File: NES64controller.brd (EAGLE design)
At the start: 113 x 45.7 mm, 10 parts, among them CN1 NES64_CONNECTOR

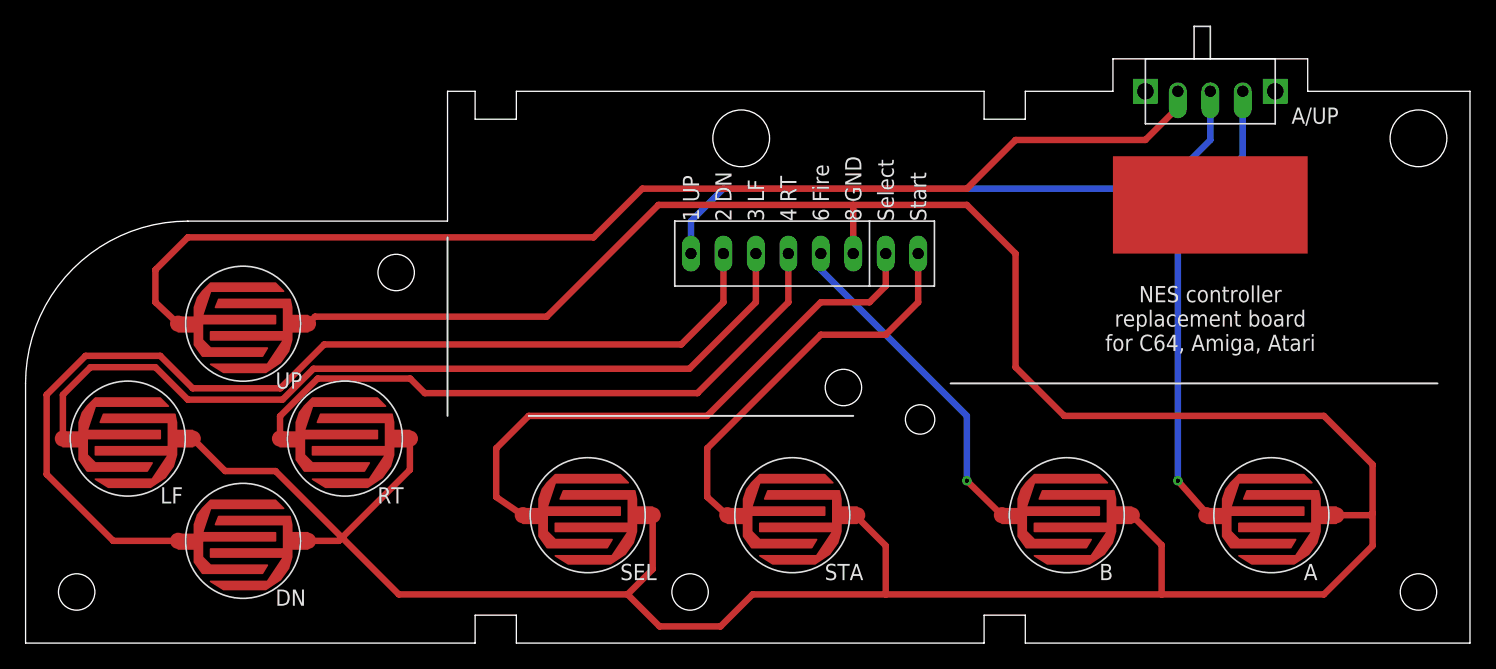
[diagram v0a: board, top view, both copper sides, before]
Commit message: Adjustment of hole size in lower right corner and edge notches to fit USB controller case; slight correcting translation of top holes and middle small hole downwards; removing small area of solder mask from middle of button contact areas; adjusting distance between switch pads
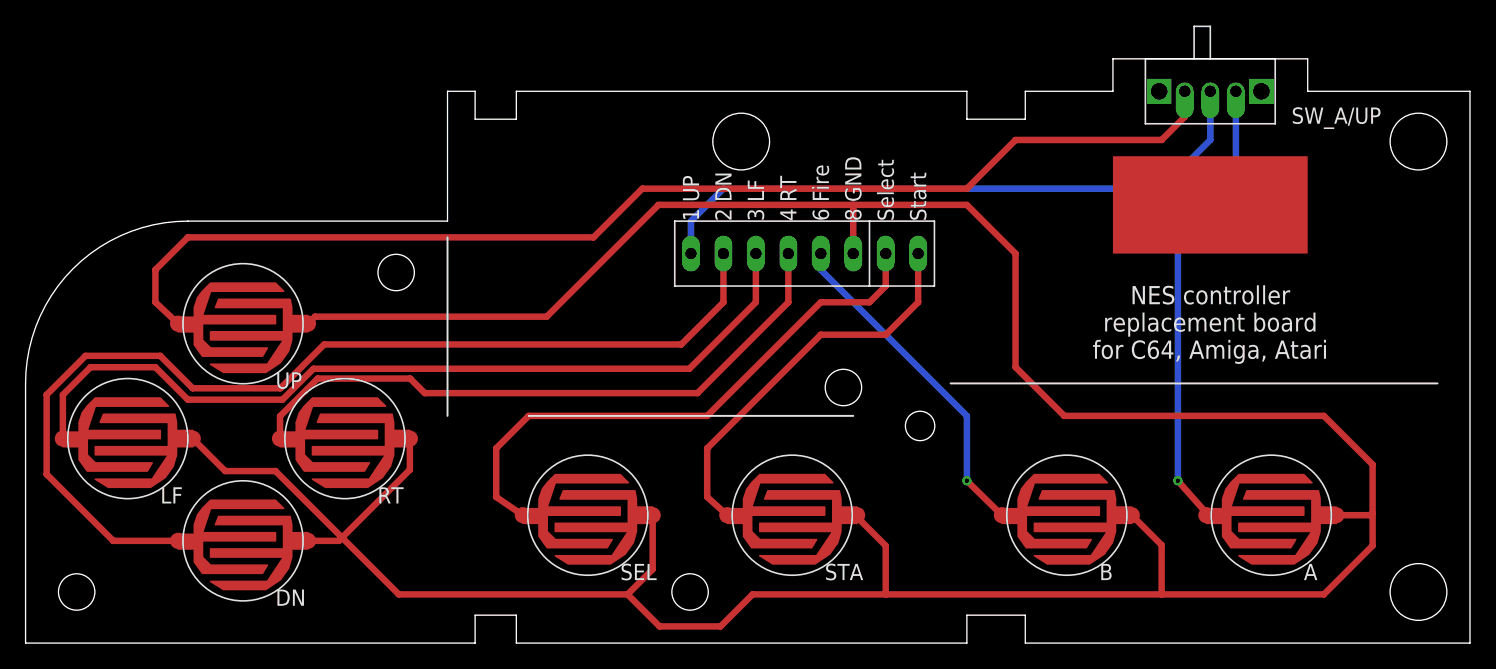
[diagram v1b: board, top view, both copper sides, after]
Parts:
- renumbered A/UP to SW_A/UP
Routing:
- net N$9: track 91.5 -> 92.5 mm
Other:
- outline, holes or cut-outs redrawn
- board text added: "version 0.2"
- board text removed: "version 0.1"
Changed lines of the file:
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@@
 <layers>
 <layer number="1" name="Top" color="4" fill="1" visible="yes" active="yes"/>
-<layer number="16" name="Bottom" color="1" fill="1" visible="no" active="yes"/>
+<layer number="16" name="Bottom" color="1" fill="1" visible="yes" active="yes"/>
 <layer number="17" name="Pads" color="2" fill="1" visible="yes" active="yes"/>
 <layer number="18" name="Vias" color="2" fill="1" visible="yes" active="yes"/>
@@
 <layer number="20" name="Dimension" color="24" fill="1" visible="yes" active="yes"/>
 <layer number="21" name="tPlace" color="7" fill="1" visible="yes" active="yes"/>
-<layer number="22" name="bPlace" color="7" fill="1" visible="no" active="yes"/>
+<layer number="22" name="bPlace" color="7" fill="1" visible="yes" active="yes"/>
 <layer number="23" name="tOrigins" color="15" fill="1" visible="yes" active="yes"/>
-<layer number="24" name="bOrigins" color="15" fill="1" visible="no" active="yes"/>
+<layer number="24" name="bOrigins" color="15" fill="1" visible="yes" active="yes"/>
 <layer number="25" name="tNames" color="7" fill="1" visible="yes" active="yes"/>
-<layer number="26" name="bNames" color="7" fill="1" visible="no" active="yes"/>
+<layer number="26" name="bNames" color="7" fill="1" visible="yes" active="yes"/>
 <layer number="27" name="tValues" color="7" fill="1" visible="yes" active="yes"/>
-<layer number="28" name="bValues" color="7" fill="1" visible="no" active="yes"/>
+<layer number="28" name="bValues" color="7" fill="1" visible="yes" active="yes"/>
 <layer number="29" name="tStop" color="7" fill="3" visible="yes" active="yes"/>
 <layer number="30" name="bStop" color="7" fill="6" visible="no" active="yes"/>
@@
 <wire x1="35.179" y1="2.1844" x2="38.4048" y2="2.1844" width="0" layer="20"/>
 <wire x1="38.4048" y1="2.1844" x2="38.4048" y2="0" width="0" layer="20"/>
-<wire x1="38.4048" y1="0" x2="75.0062" y2="0" width="0" layer="20"/>
-<wire x1="75.0062" y1="0" x2="75.0062" y2="2.1844" width="0" layer="20"/>
-<wire x1="75.0062" y1="2.1844" x2="78.232" y2="2.1844" width="0" layer="20"/>
+<wire x1="38.4048" y1="0" x2="73.66" y2="0" width="0" layer="20"/>
+<wire x1="73.66" y1="0" x2="73.66" y2="2.1844" width="0" layer="20"/>
+<wire x1="73.66" y1="2.1844" x2="78.232" y2="2.1844" width="0" layer="20"/>
 <wire x1="78.232" y1="2.1844" x2="78.232" y2="0" width="0" layer="20"/>
 <wire x1="78.232" y1="0" x2="113.03" y2="0" width="0" layer="20"/>
@@
 <wire x1="85.09" y1="43.18" x2="78.232" y2="43.18" width="0" layer="20"/>
 <wire x1="78.232" y1="43.18" x2="78.232" y2="40.9956" width="0" layer="20"/>
-<wire x1="78.232" y1="40.9956" x2="75.0062" y2="40.9956" width="0" layer="20"/>
-<wire x1="75.0062" y1="40.9956" x2="75.0062" y2="43.18" width="0" layer="20"/>
-<wire x1="75.0062" y1="43.18" x2="38.4048" y2="43.18" width="0" layer="20"/>
+<wire x1="78.232" y1="40.9956" x2="73.66" y2="40.9956" width="0" layer="20"/>
+<wire x1="73.66" y1="40.9956" x2="73.66" y2="43.18" width="0" layer="20"/>
+<wire x1="73.66" y1="43.18" x2="38.4048" y2="43.18" width="0" layer="20"/>
 <wire x1="38.4048" y1="43.18" x2="38.4048" y2="40.9956" width="0" layer="20"/>
 <wire x1="38.4048" y1="40.9956" x2="35.179" y2="40.9956" width="0" layer="20"/>
@@
 <hole x="4" y="4" drill="2.85"/>
 <hole x="52" y="4" drill="2.85"/>
-<hole x="109" y="4" drill="2.85"/>
-<hole x="109" y="39.5" drill="4.44"/>
-<hole x="56" y="39.5" drill="4.44"/>
+<hole x="109" y="4" drill="4.44"/>
+<hole x="109" y="39.246" drill="4.44"/>
+<hole x="56" y="39.246" drill="4.44"/>
 <hole x="29" y="29" drill="2.85"/>
 <hole x="64" y="20" drill="2.85"/>
-<hole x="70" y="17.5" drill="2.3"/>
+<hole x="70" y="16.992" drill="2.3"/>
 <wire x1="39.37" y1="17.78" x2="64.77" y2="17.78" width="0.1524" layer="21"/>
 <wire x1="72.39" y1="20.32" x2="110.49" y2="20.32" width="0.1524" layer="21"/>
 <wire x1="33.02" y1="31.75" x2="33.02" y2="17.78" width="0.1524" layer="21"/>
-<text x="92.71" y="27.94" size="1.27" layer="21" align="top-center">NES controller
+<text x="92.71" y="27.94" size="1.4224" layer="21" align="top-center">NES controller
 replacement board
 for C64, Amiga, Atari</text>
 <rectangle x1="85.09" y1="30.48" x2="100.33" y2="38.1" layer="1"/>
 <text x="92.71" y="36.83" size="2.54" layer="29" align="top-center">NES64</text>
-<text x="92.71" y="31.75" size="1.778" layer="29" align="bottom-center">version 0.1</text>
+<text x="92.71" y="31.75" size="1.778" layer="29" align="bottom-center">version 0.2</text>
 <wire x1="22.86" y1="16.51" x2="10.16" y2="16.51" width="0.508" layer="22"/>
 <wire x1="10.16" y1="16.51" x2="11.43" y2="11.43" width="0.508" layer="22"/>
@@
 <wire x1="30.48" y1="30.48" x2="50.8" y2="30.48" width="0.1524" layer="22"/>
 <text x="1.27" y="45.72" size="1.778" layer="51" align="top-left">Board thickness: 1.6 mm</text>
-<text x="106.68" y="13.97" size="1.27" layer="22" rot="MR0">For use in NES controller to make it
+<text x="106.68" y="13.97" size="1.4224" layer="22" rot="MR0">For use in NES controller to make it
 compatible with Commodore 64,
 Amiga, and other computers using
@@
 <attribute name="NAME" x="19.558" y="21.1836" size="1.27" layer="25" align="top-left"/>
 </element>
-<element name="A/UP" library="Thomas" package="TOGGLESWITCH_SPDT_SMALL_90DEG" value="TOGGLESWITCH_SPDT_SMALL_90DEG" x="92.71" y="43.18" smashed="yes">
+<element name="SW_A/UP" library="Thomas" package="TOGGLESWITCH_SPDT_SMALL_90DEG" value="TOGGLESWITCH_SPDT_SMALL_90DEG" x="92.71" y="43.18" smashed="yes">
 <attribute name="NAME" x="99.06" y="40.64" size="1.27" layer="25"/>
 </element>
@@
 <signal name="N$9">
 <contactref element="UP" pad="A"/>
-<contactref element="A/UP" pad="A"/>
+<contactref element="SW_A/UP" pad="A"/>
 <wire x1="11.938" y1="24.9936" x2="10.16" y2="26.67" width="0.508" layer="1"/>
 <wire x1="10.16" y1="29.21" x2="10.16" y2="26.67" width="0.508" layer="1"/>
-<wire x1="77.47" y1="39.37" x2="73.66" y2="35.56" width="0.508" layer="1"/>
-<wire x1="87.63" y1="39.37" x2="77.47" y2="39.37" width="0.508" layer="1"/>
-<wire x1="90.17" y1="43.18" x2="90.17" y2="41.91" width="0.508" layer="1"/>
-<wire x1="90.17" y1="41.91" x2="87.63" y2="39.37" width="0.508" layer="1"/>
+<wire x1="73.66" y1="35.56" x2="77.47" y2="39.37" width="0.508" layer="1"/>
 <wire x1="48.26" y1="35.56" x2="44.45" y2="31.75" width="0.508" layer="1"/>
 <wire x1="73.66" y1="35.56" x2="48.26" y2="35.56" width="0.508" layer="1"/>
 <wire x1="44.45" y1="31.75" x2="12.7" y2="31.75" width="0.508" layer="1"/>
 <wire x1="12.7" y1="31.75" x2="10.16" y2="29.21" width="0.508" layer="1"/>
+<wire x1="77.47" y1="39.37" x2="88.9" y2="39.37" width="0.508" layer="1"/>
+<wire x1="88.9" y1="39.37" x2="90.71" y2="41.18" width="0.508" layer="1"/>
+<wire x1="90.71" y1="41.18" x2="90.71" y2="43.18" width="0.508" layer="1"/>
 </signal>
 <signal name="N$4">
@@
 <signal name="N$10">
 <contactref element="A" pad="A"/>
-<contactref element="A/UP" pad="B"/>
+<contactref element="SW_A/UP" pad="B"/>
 <wire x1="92.4052" y1="10.0076" x2="92.4052" y2="10.173253125" width="0.508" layer="1"/>
 <via x="90.17" y="12.7" extent="1-16" drill="0.35"/>
 <wire x1="90.17" y1="12.7" x2="90.17" y2="33.02" width="0.508" layer="16"/>
-<wire x1="90.17" y1="33.02" x2="95.25" y2="38.1" width="0.508" layer="16"/>
-<wire x1="95.25" y1="38.1" x2="95.25" y2="43.18" width="0.508" layer="16"/>
 <wire x1="92.4052" y1="10.173253125" x2="90.17" y2="12.7" width="0.508" layer="1"/>
+<wire x1="90.17" y1="33.02" x2="94.71" y2="37.56" width="0.508" layer="16"/>
+<wire x1="94.71" y1="37.56" x2="94.71" y2="43.18" width="0.508" layer="16"/>
 </signal>
 <signal name="N$2">
-<contactref element="A/UP" pad="N"/>
+<contactref element="SW_A/UP" pad="N"/>
 <contactref element="CN1" pad="1UP"/>
 <wire x1="52.07" y1="30.48" x2="52.07" y2="33.02" width="0.508" layer="16"/>
